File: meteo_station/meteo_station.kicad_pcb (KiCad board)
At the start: 2 copper layers, 110 x 90 mm, 24 parts, among them SW1 SW_SPDT, U1 TP4056, U2 LF33_TO220, U3 ESP32-WROOM, U4 DS18B20, U5 BH1750, U6 BME280

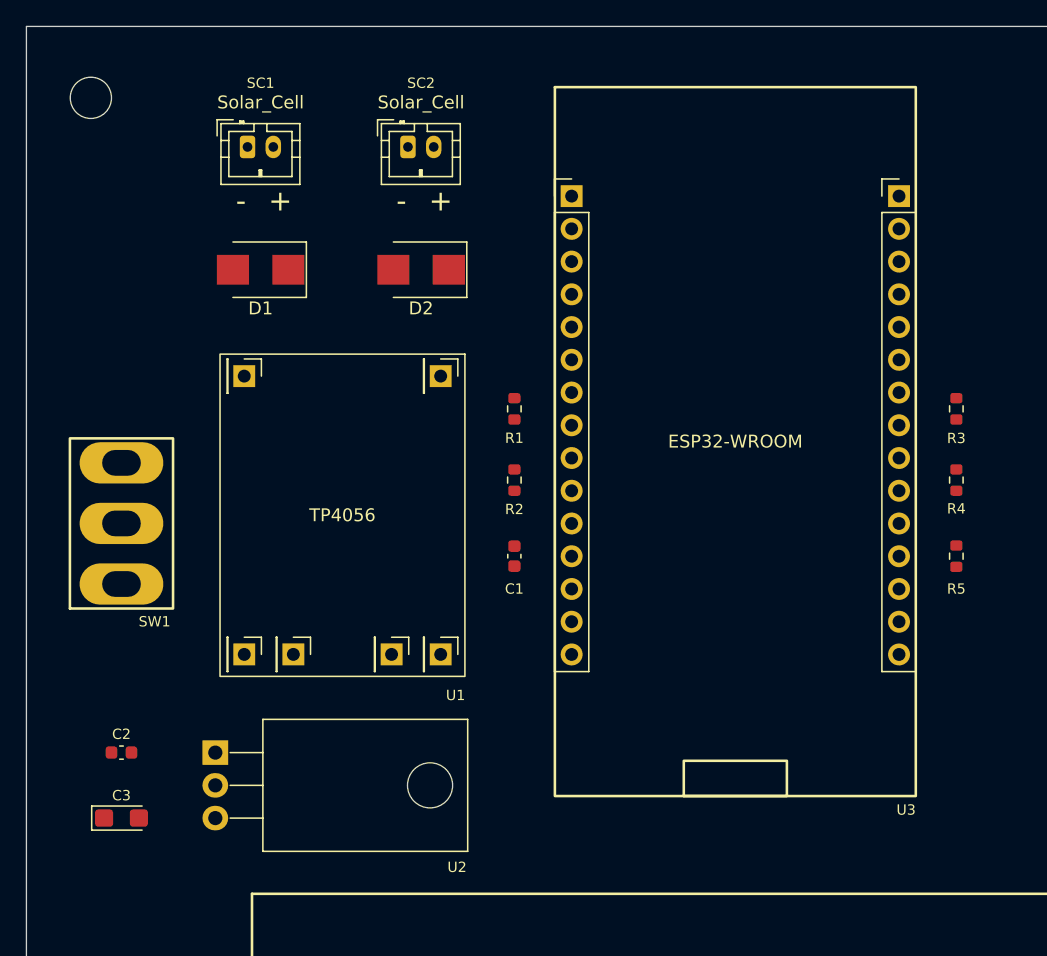
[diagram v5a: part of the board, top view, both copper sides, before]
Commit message: Change rotation to make USBs visible
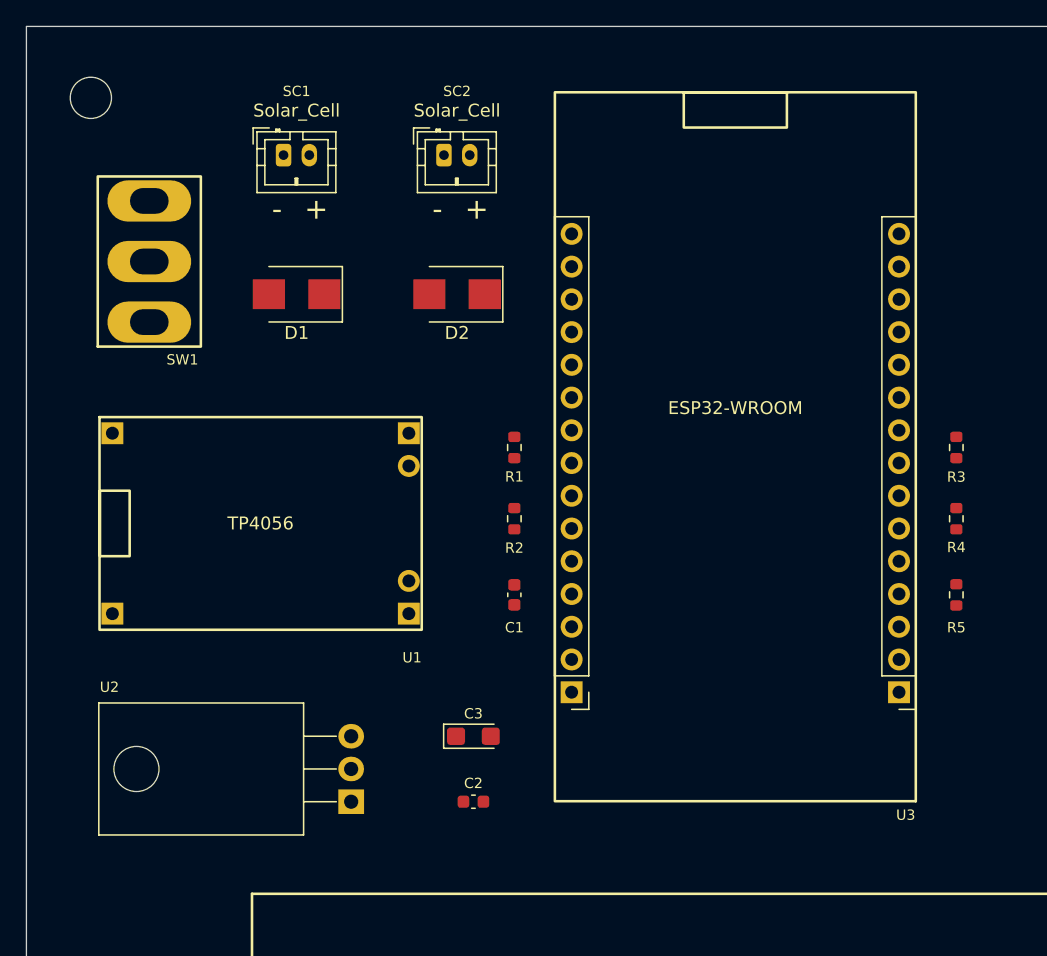
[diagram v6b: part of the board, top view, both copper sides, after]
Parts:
- moved C3 28.0 mm to (129.5, 115.6)
- moved C2 27.6 mm to (129.5, 120.7)
- moved SW1 20.4 mm to (104.4, 78.7)
- moved U2 11.2 mm to (120.1, 120.7), turned to 90 degrees
- moved U1 6.38 mm to (113.0, 99.1), turned to 0 degrees
- moved D2 3.38 mm to (128.3, 81.3)
- moved D1 3.38 mm to (115.8, 81.3)
- moved C1 3.00 mm to (132.7, 104.6)
- moved R1 3.00 mm to (132.7, 93.2)
- moved R2 3.00 mm to (132.7, 98.7)
- moved R3 3.00 mm to (167.0, 93.2)
- moved R4 3.00 mm to (167.0, 98.7)
- moved R5 3.00 mm to (167.0, 104.6)
- moved SC2 2.87 mm to (128.3, 71.1)
- moved SC1 2.87 mm to (115.8, 71.1)
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
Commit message: Add some routing
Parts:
- turned R5 to -90 degrees
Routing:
- net 3V3: track 0.00 -> 125.5 mm
- net SDA: track 0.00 -> 95.4 mm, vias 0 -> 1
- net Net-(BT1-Pad1): track 0.00 -> 94.4 mm
- net OUT+: track 0.00 -> 86.8 mm, vias 0 -> 1
- net SCL: track 0.00 -> 74.2 mm, vias 0 -> 1
- net Net-(SC1-Pad2): track 0.00 -> 74.0 mm
- net OUT-: track 0.00 -> 59.7 mm, vias 0 -> 2
- net Net-(D1-Pad1): track 0.00 -> 59.7 mm, vias 0 -> 2
- net BAT_V: track 0.00 -> 52.0 mm
- net Net-(BT1-Pad2): track 0.00 -> 45.3 mm
- net Net-(R5-Pad2): track 0.00 -> 36.3 mm, vias 0 -> 2
- net Net-(SW1-Pad2): track 0.00 -> 25.7 mm
- net Net-(D2-Pad2): track 0.00 -> 11.3 mm
- net Net-(D1-Pad2): track 0.00 -> 11.3 mm

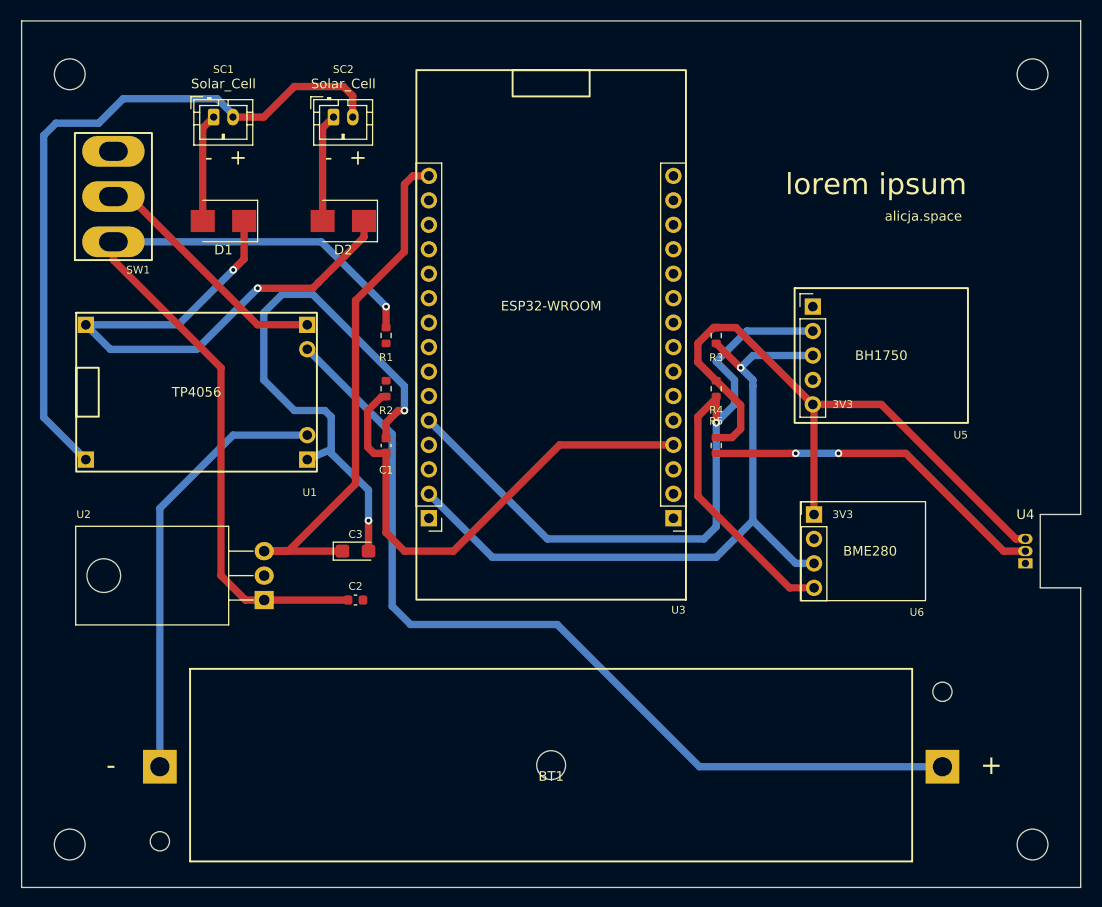
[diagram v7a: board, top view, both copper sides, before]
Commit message: Start working on logo
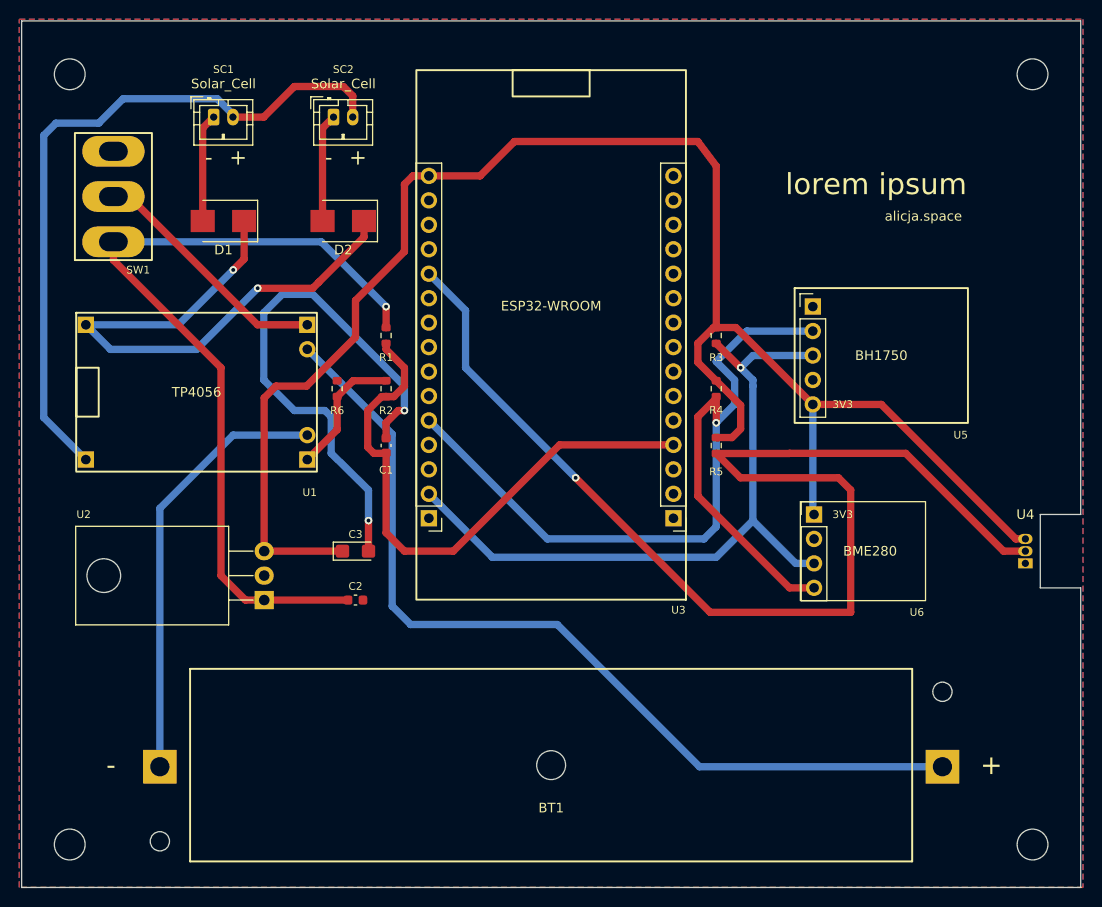
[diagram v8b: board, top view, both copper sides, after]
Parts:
- added G***: LOGO, meteo_station_footprints:logo_kicad, B.Cu at (148.6, 99.7)
- added R6: 0R, Resistor_SMD:R_0603_1608Metric, F.Cu at (127.6, 98.7)
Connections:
- C1 pad 2: OUT- -> GND
- C2 pad 2: OUT- -> GND
- C3 pad 2: OUT- -> GND
- U2 pad 2: OUT- -> GND
- U3 pad 14: OUT- -> GND
- U3 pad 29: OUT- -> GND
- U4 pad 1: OUT- -> GND
- U5 pad 2: OUT- -> GND
- U5 pad 5: OUT- -> GND
- U6 pad 2: OUT- -> GND
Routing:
- net Net-(R5-Pad2): track 36.3 -> 126.4 mm, vias 2 -> 1
- net GND: track 0.00 -> 57.0 mm, vias 0 -> 2
- net 3V3: track 125.5 -> 175.3 mm
- net OUT-: track 59.7 -> 13.6 mm, vias 2 -> 0
- net BAT_V: track 52.0 -> 59.6 mm
- added copper zone on B.Cu, net GND
- added copper zone on F.Cu, net GND
